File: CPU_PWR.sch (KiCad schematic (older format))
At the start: 44 parts

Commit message: Prepare for two battery types NiMH battery for using the original battery pack LiPo battery for using long lasting modern battery
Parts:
- gave numbers to parts that had none: 43

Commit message: Modified power nets Added table of contents
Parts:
- added R?: 0R, symbol R
- added TP? (x8): TP, symbol TP
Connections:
- net labels added: NVCC_GPIO
- net labels removed: VDDA_1P0_CAP, VDDA_PHY_1P6, VDD_1P0_CAP, VDD_1P2_CAP, VDD_SNVS_1P8_CAP
- wire segments 301 -> 302
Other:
- moved on the sheet: C1223, C1230, C1232

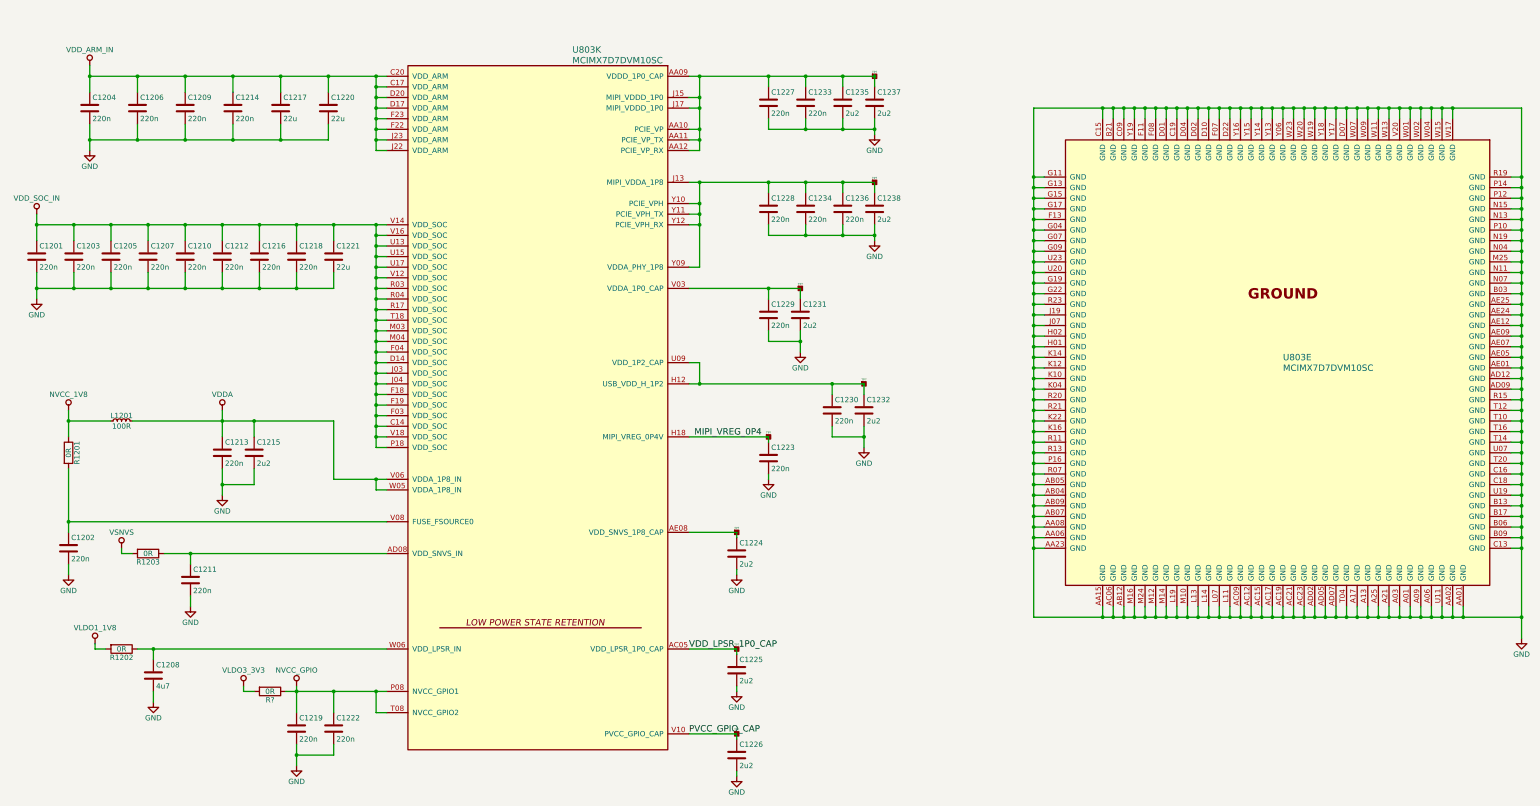
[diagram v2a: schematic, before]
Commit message: Changed several voltage rail connections Removed non existing rails Added circuit for NiMH charging
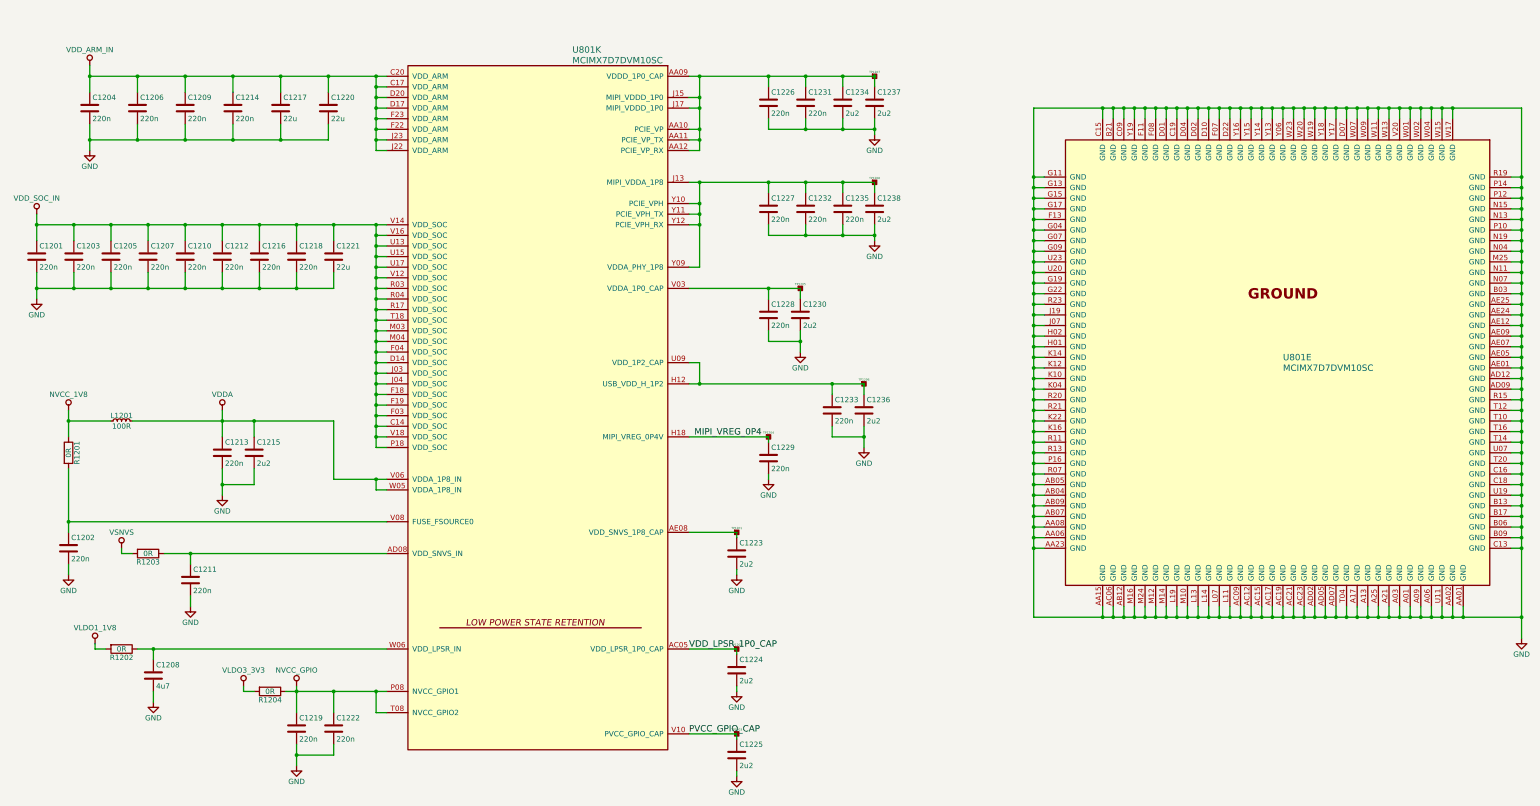
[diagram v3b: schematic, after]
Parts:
- gave numbers to parts that had none: 9
- renumbered C1224 to C1223, C1225 to C1224, C1226 to C1225, C1227 to C1226, C1228 to C1227, C1229 to C1228, C1223 to C1229, C1231 to C1230, C1233 to C1231, C1234 to C1232, C1230 to C1233, C1235 to C1234, C1236 to C1235, C1232 to C1236, U803 to U801

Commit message: Created netlist with current components Foreward Annotation to Board
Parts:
- C1201, C1202, C1203, C1204, C1205, C1206, C1207, C1209, C1210, C1211, C1212, C1213, C1214, C1216, C1218, C1219, C1222, C1226, C1227, C1228, C1229, C1231, C1232, C1233, C1235: footprint (none) -> Capacitors_SMD:C_0402
- C1208, C1215, C1217, C1220, C1221, C1223, C1224, C1225, C1230, C1234, C1236, C1237, C1238: footprint (none) -> Capacitors_SMD:C_0603
- L1201: footprint Resistors_SMD:R_0603 -> Choke_SMD:Choke_SMD_1206_Standard
- R1201, R1202, R1203, R1204: footprint (none) -> Resistors_SMD:R_0402
- TP1201, TP1202, TP1203, TP1204, TP1205, TP1206, TP1207, TP1208: footprint (none) -> NokiaRetroFit:TP
- U801: footprint (none) -> NokiaRetroFit:BGA_541_075_19x19
